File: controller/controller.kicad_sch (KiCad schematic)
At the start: 5 parts, among them IC1 74HC154BQ,118, J5 Screw_Terminal_01x03, U1 PBO-3E-12, U2 LM7805_TO220

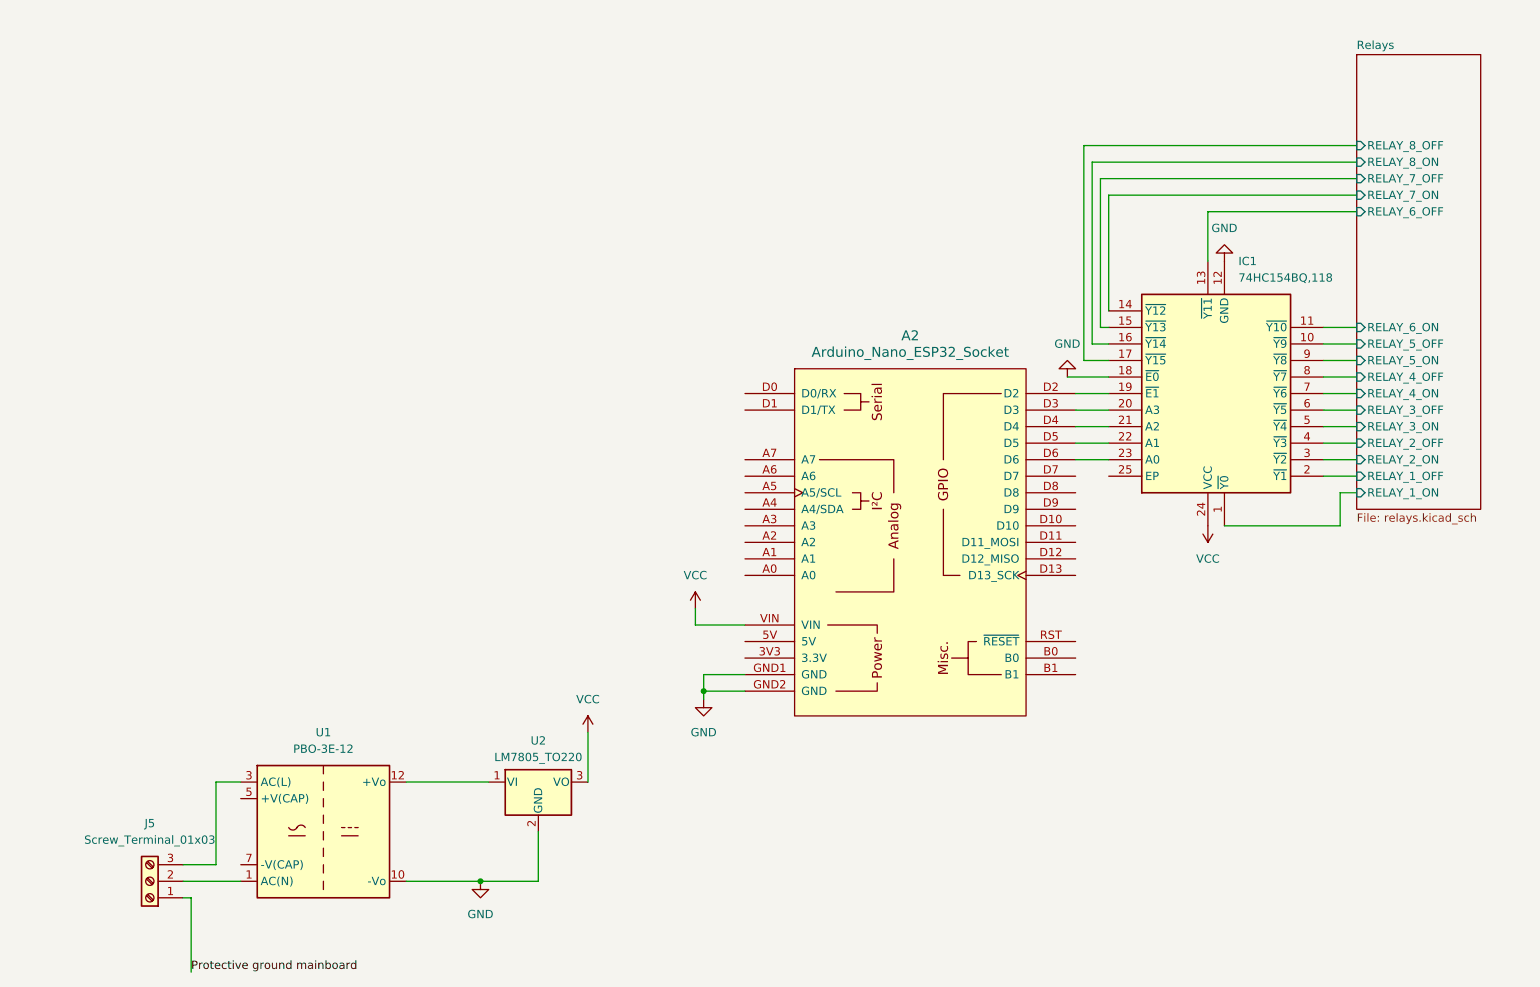
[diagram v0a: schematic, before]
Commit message: made symbols and footprint relative to project
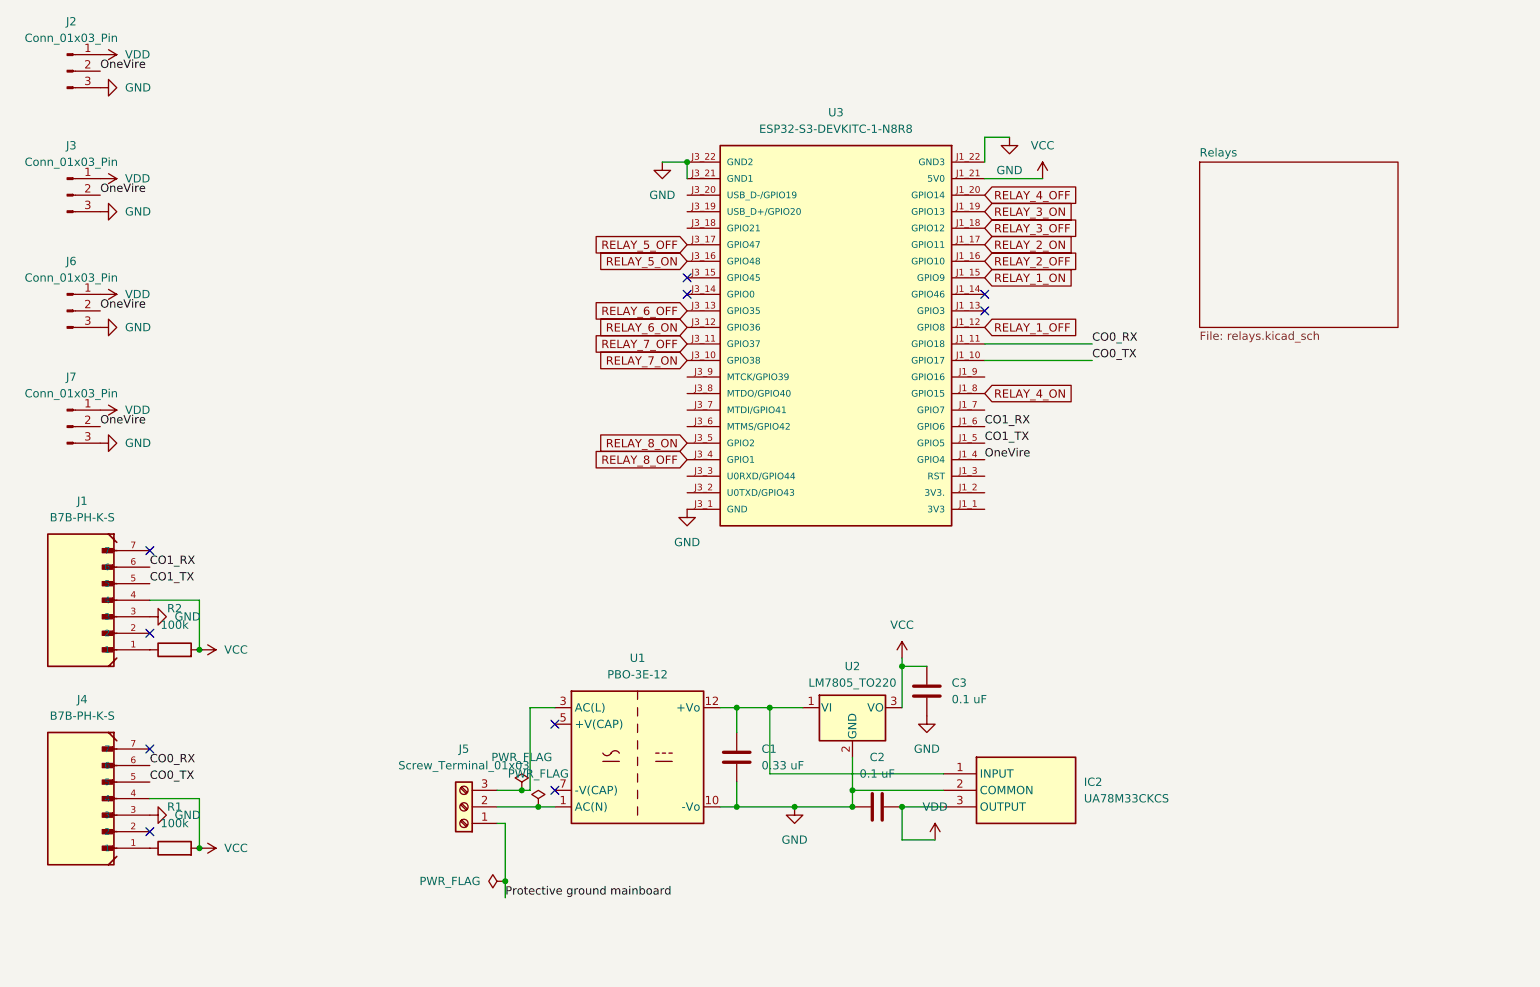
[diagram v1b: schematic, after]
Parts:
- removed A2: Arduino_Nano_ESP32_Socket, arduino-library:Arduino_Nano_ESP32_Socket, symbol arduino-library:Arduino_Nano_ESP32_Socket
- removed IC1: 74HC154BQ,118, 74HC154BQ118, symbol 74HC154BQ_118:74HC154BQ,118
- added C1: 0.33 uF, symbol Device:C
- added C2, C3: 0.1 uF, symbol Device:C
- added IC2: UA78M33CKCS, arduino-library:TO254P470X1016X1965-3P, symbol UA78M33CKCS:UA78M33CKCS
- added J1, J4: B7B-PH-K-S, arduino-library:JST_B7B-PH-K-S, symbol B7B-PH-K-S:B7B-PH-K-S
- added J2, J3, J6, J7: Conn_01x03_Pin, Connector_PinHeader_2.54mm:PinHeader_1x03_P2.54mm_Vertical, symbol Connector:Conn_01x03_Pin
- added R1, R2: 100k, symbol Device:R
- added U3: ESP32-S3-DEVKITC-1-N8R8, arduino-library:ESP32-S3-DEVKITC-1-N8R8, symbol ESP32-S3-DEVKITC-1-N8R8:ESP32-S3-DEVKITC-1-N8R8
- J5: footprint (none) -> arduino-library:TBL00138103GY2GY
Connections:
- net GND: now also C1.1, C2.1, C3.1, IC2.2 (COMMON), J1.3, J2.3 (Pin_3), J3.3 (Pin_3), J4.3, J6.3 (Pin_3), J7.3 (Pin_3), U3.J1_22 (GND3), U3.J3_1 (GND), U3.J3_21 (GND1), U3.J3_22 (GND2)
- net VCC: now also C3.2, J1.4, J4.4, R1.2, R2.2, U3.J1_21 (5V0)
- net at U1.12 (+Vo), U2.1 (VI): now also C1.2, IC2.1 (INPUT)
- new net: J4.1, R1.1
- new net: J1.1, R2.1
- new net CO0_RX: J4.6, U3.J1_11 (GPIO18)
- new net CO0_TX: J4.5, U3.J1_10 (GPIO17)
- new net CO1_RX: J1.6, U3.J1_6 (GPIO6)
- new net CO1_TX: J1.5, U3.J1_5 (GPIO5)
- new net OneVire: J2.2 (Pin_2), J3.2 (Pin_2), J6.2 (Pin_2), J7.2 (Pin_2), U3.J1_4 (GPIO4)
- new net RELAY_1_OFF: U3.J1_12 (GPIO8)
- new net RELAY_1_ON: U3.J1_15 (GPIO9)
- new net RELAY_2_OFF: U3.J1_16 (GPIO10)
- new net RELAY_2_ON: U3.J1_17 (GPIO11)
- new net RELAY_3_OFF: U3.J1_18 (GPIO12)
- new net RELAY_3_ON: U3.J1_19 (GPIO13)
- new net RELAY_4_OFF: U3.J1_20 (GPIO14)
- new net RELAY_4_ON: U3.J1_8 (GPIO15)
- new net RELAY_5_OFF: U3.J3_17 (GPIO47)
- new net RELAY_5_ON: U3.J3_16 (GPIO48)
- new net RELAY_6_OFF: U3.J3_13 (GPIO35)
- new net RELAY_6_ON: U3.J3_12 (GPIO36)
- new net RELAY_7_OFF: U3.J3_11 (GPIO37)
- new net RELAY_7_ON: U3.J3_10 (GPIO38)
- new net RELAY_8_OFF: U3.J3_4 (GPIO1)
- new net RELAY_8_ON: U3.J3_5 (GPIO2)
- new net VDD: C2.2, IC2.3 (OUTPUT), J2.1 (Pin_1), J3.1 (Pin_1), J6.1 (Pin_1), J7.1 (Pin_1)
- no-connect marks 0 -> 10
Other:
- sheet Relays ports: added none; removed RELAY_1_OFF, RELAY_1_ON, RELAY_2_OFF, RELAY_2_ON, RELAY_3_OFF, RELAY_3_ON, RELAY_4_OFF, RELAY_4_ON, RELAY_5_OFF, RELAY_5_ON, RELAY_6_OFF, RELAY_6_ON, RELAY_7_OFF, RELAY_7_ON, RELAY_8_OFF, RELAY_8_ON
- moved on the sheet: J5, U1, U2
